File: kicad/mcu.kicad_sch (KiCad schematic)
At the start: 32 parts, among them J8 USB_C_Receptacle_USB2.0_14P, J9 Conn_01x03, SW1 SW_Push, SW2 SW_Push, U12 ESP32-S3-WROOM-1-N8R2

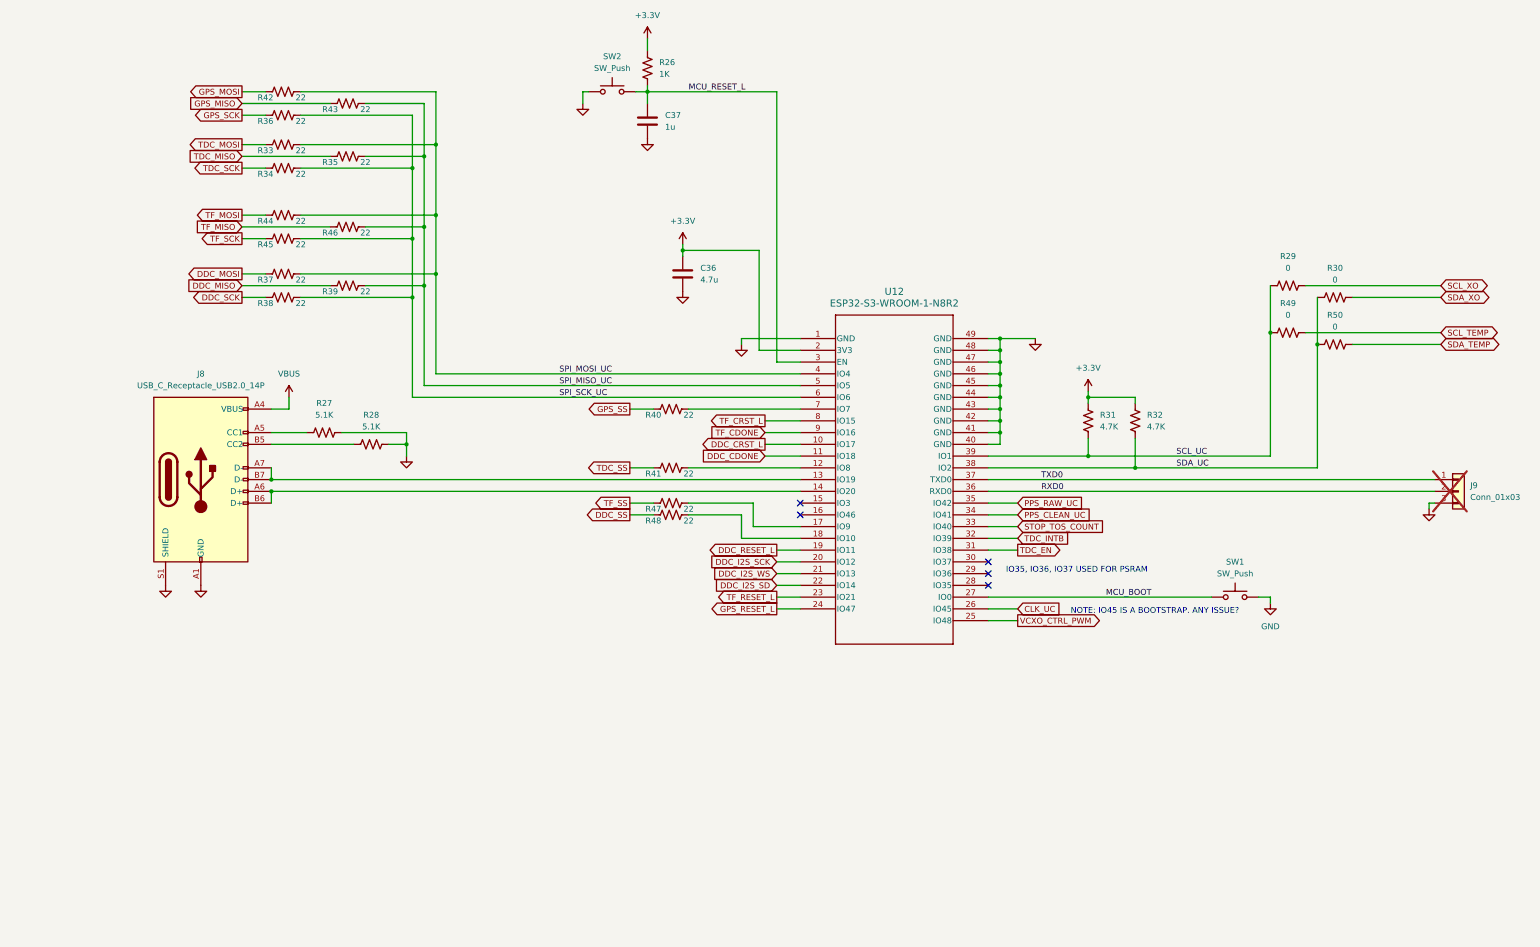
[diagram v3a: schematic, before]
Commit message: add tcxo
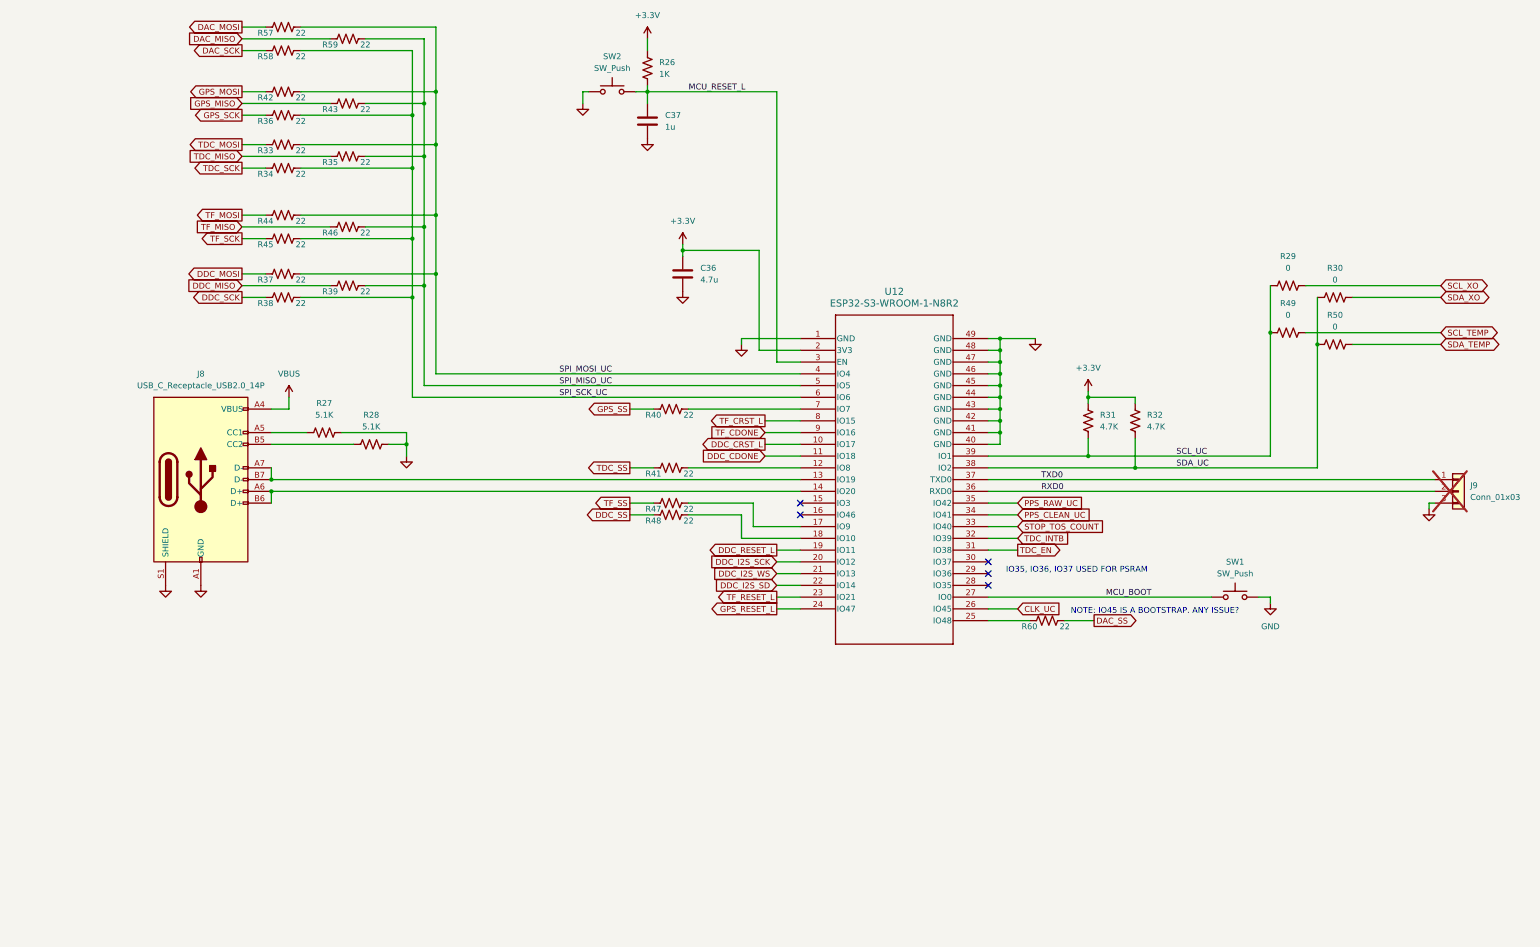
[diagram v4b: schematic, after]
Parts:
- added R57, R58, R59, R60: 22, symbol Device:R_US
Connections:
- net SPI_MISO_UC: now also R59.2
- net SPI_MOSI_UC: now also R57.2
- net SPI_SCK_UC: now also R58.2
- net VCXO_CTRL_PWM: no longer names the net of U12.25 (IO48)
- net VCXO_CTRL_PWM: now also R60.1
- new net DAC_MISO: R59.1
- new net DAC_MOSI: R57.1
- new net DAC_SCK: R58.1
- new net DAC_SS: R60.2
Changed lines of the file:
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@@
   (junction (at 229.87 120.65) (diameter 0) (color 0 0 0 0)
   )
+  (junction (at 105.41 54.61) (diameter 0) (color 0 0 0 0)
+  )
+  (junction (at 102.87 57.15) (diameter 0) (color 0 0 0 0)
+  )
   (junction (at 229.87 110.49) (diameter 0) (color 0 0 0 0)
   )
@@
   )
   (junction (at 248.92 130.81) (diameter 0) (color 0 0 0 0)
+  )
+  (junction (at 107.95 52.07) (diameter 0) (color 0 0 0 0)
   )
   (junction (at 102.87 68.58) (diameter 0) (color 0 0 0 0)
@@
     (stroke (width 0) (type default))
   )
+  (wire (pts (xy 66.04 38.1) (xy 71.12 38.1))
+    (stroke (width 0) (type default))
+  )
   (wire (pts (xy 227.33 125.73) (xy 229.87 125.73))
     (stroke (width 0) (type default))
@@
     (stroke (width 0) (type default))
   )
+  (wire (pts (xy 66.04 43.18) (xy 71.12 43.18))
+    (stroke (width 0) (type default))
+  )
   (wire (pts (xy 181.61 52.07) (xy 181.61 110.49))
     (stroke (width 0) (type default))
@@
     (stroke (width 0) (type default))
   )
+  (wire (pts (xy 227.33 166.37) (xy 236.22 166.37))
+    (stroke (width 0) (type default))
+  )
   (wire (pts (xy 151.13 52.07) (xy 153.67 52.07))
     (stroke (width 0) (type default))
@@
     (stroke (width 0) (type default))
   )
+  (wire (pts (xy 92.71 40.64) (xy 105.41 40.64))
+    (stroke (width 0) (type default))
+  )
   (wire (pts (xy 177.8 107.95) (xy 177.8 86.36))
     (stroke (width 0) (type default))
@@
     (stroke (width 0) (type default))
   )
-  (wire (pts (xy 227.33 166.37) (xy 233.68 166.37))
-    (stroke (width 0) (type default))
-  )
   (wire (pts (xy 298.45 133.35) (xy 259.08 133.35))
     (stroke (width 0) (type default))
@@
     (stroke (width 0) (type default))
   )
+  (wire (pts (xy 107.95 38.1) (xy 107.95 52.07))
+    (stroke (width 0) (type default))
+  )
   (wire (pts (xy 72.39 138.43) (xy 186.69 138.43))
     (stroke (width 0) (type default))
   )
+  (wire (pts (xy 105.41 40.64) (xy 105.41 54.61))
+    (stroke (width 0) (type default))
+  )
   (wire (pts (xy 227.33 148.59) (xy 233.68 148.59))
     (stroke (width 0) (type default))
@@
     (stroke (width 0) (type default))
   )
+  (wire (pts (xy 66.04 40.64) (xy 85.09 40.64))
+    (stroke (width 0) (type default))
+  )
   (wire (pts (xy 78.74 91.44) (xy 107.95 91.44))
     (stroke (width 0) (type default))
@@
     (stroke (width 0) (type default))
   )
+  (wire (pts (xy 78.74 43.18) (xy 102.87 43.18))
+    (stroke (width 0) (type default))
+  )
+  (wire (pts (xy 102.87 43.18) (xy 102.87 57.15))
+    (stroke (width 0) (type default))
+  )
   (wire (pts (xy 78.74 78.74) (xy 107.95 78.74))
     (stroke (width 0) (type default))
@@
     (stroke (width 0) (type default))
   )
+  (wire (pts (xy 243.84 166.37) (xy 250.19 166.37))
+    (stroke (width 0) (type default))
+  )
   (wire (pts (xy 78.74 63.5) (xy 107.95 63.5))
     (stroke (width 0) (type default))
@@
   )
   (wire (pts (xy 229.87 110.49) (xy 229.87 107.95))
+    (stroke (width 0) (type default))
+  )
+  (wire (pts (xy 78.74 38.1) (xy 107.95 38.1))
     (stroke (width 0) (type default))
   )
@@
     )
   )
+  (global_label "DAC_SCK" (shape output) (at 66.04 43.18 180) (fields_autoplaced)
+    (effects (font (size 1.27 1.27)) (justify right))
+    (property "Intersheetrefs" "${INTERSHEET_REFS}" (at 54.7091 43.18 0)
+      (effects (font (size 1.27 1.27)) (justify right) hide)
+    )
+  )
   (global_label "TDC_SCK" (shape output) (at 66.04 68.58 180) (fields_autoplaced)
     (effects (font (size 1.27 1.27)) (justify right))
@@
     )
   )
-  (global_label "VCXO_CTRL_PWM" (shape output) (at 233.68 166.37 0) (fields_autoplaced)
+  (global_label "DAC_SS" (shape output) (at 250.19 166.37 0) (fields_autoplaced)
     (effects (font (size 1.27 1.27)) (justify left))
-    (property "Intersheetrefs" "${INTERSHEET_REFS}" (at 252.2075 166.37 0)
+    (property "Intersheetrefs" "${INTERSHEET_REFS}" (at 260.1904 166.37 0)
       (effects (font (size 1.27 1.27)) (justify left) hide)
     )
@@
     (effects (font (size 1.27 1.27)) (justify right))
     (property "Intersheetrefs" "${INTERSHEET_REFS}" (at 53.7415 54.61 0)
+      (effects (font (size 1.27 1.27)) (justify right) hide)
+    )
+  )
+  (global_label "DAC_MISO" (shape input) (at 66.04 40.64 180) (fields_autoplaced)
+    (effects (font (size 1.27 1.27)) (justify right))
+    (property "Intersheetrefs" "${INTERSHEET_REFS}" (at 53.8624 40.64 0)
       (effects (font (size 1.27 1.27)) (justify right) hide)
     )
@@
     (effects (font (size 1.27 1.27)) (justify right))
     (property "Intersheetrefs" "${INTERSHEET_REFS}" (at 54.5277 96.52 0)
+      (effects (font (size 1.27 1.27)) (justify right) hide)
+    )
+  )
+  (global_label "DAC_MOSI" (shape output) (at 66.04 38.1 180) (fields_autoplaced)
+    (effects (font (size 1.27 1.27)) (justify right))
+    (property "Intersheetrefs" "${INTERSHEET_REFS}" (at 53.8624 38.1 0)
       (effects (font (size 1.27 1.27)) (justify right) hide)
     )
@@
     )
   )
+  (symbol (lib_id "Device:R_US") (at 240.03 166.37 90) (unit 1)
+    (in_bom yes) (on_board yes) (dnp no)
+    (property "Reference" "R60" (at 236.22 167.64 90)
+      (effects (font (size 1.27 1.27)))
+    )
+    (property "Value" "22" (at 243.84 167.64 90)
+      (effects (font (size 1.27 1.27)))
+    )
+    (property "Footprint" "" (at 240.284 165.354 90)
+      (effects (font (size 1.27 1.27)) hide)
+    )
+    (property "Datasheet" "~" (at 240.03 166.37 0)
+      (effects (font (size 1.27 1.27)) hide)
+    )
+    (pin "1")
+    (pin "2")
+    (instances
+      (project "gpsrx"
+        (path "/c3c549bc-9d82-4b6a-bdb9-a3870905229d/cfc19a79-2a34-431b-9452-a8a8f8302b67"
+          (reference "R60") (unit 1)
+        )
+      )
+    )
+  )
   (symbol (lib_id "power:GND") (at 57.15 158.75 0) (unit 1)
     (in_bom yes) (on_board yes) (dnp no) (fields_autoplaced)
@@
         (path "/c3c549bc-9d82-4b6a-bdb9-a3870905229d/cfc19a79-2a34-431b-9452-a8a8f8302b67"
           (reference "SW1") (unit 1)
+        )
+      )
+    )
+  )
+  (symbol (lib_id "Device:R_US") (at 88.9 40.64 90) (unit 1)
+    (in_bom yes) (on_board yes) (dnp no)
+    (property "Reference" "R59" (at 85.09 41.91 90)
+      (effects (font (size 1.27 1.27)))
+    )
+    (property "Value" "22" (at 92.71 41.91 90)
+      (effects (font (size 1.27 1.27)))
+    )
+    (property "Footprint" "" (at 89.154 39.624 90)
+      (effects (font (size 1.27 1.27)) hide)
+    )
+    (property "Datasheet" "~" (at 88.9 40.64 0)
+      (effects (font (size 1.27 1.27)) hide)
+    )
+    (pin "1")
+    (pin "2")
+    (instances
+      (project "gpsrx"
+        (path "/c3c549bc-9d82-4b6a-bdb9-a3870905229d/cfc19a79-2a34-431b-9452-a8a8f8302b67"
+          (reference "R59") (unit 1)
         )
       )
@@
     )
   )
+  (symbol (lib_id "Device:R_US") (at 74.93 38.1 90) (unit 1)
+    (in_bom yes) (on_board yes) (dnp no)
+    (property "Reference" "R57" (at 71.12 39.37 90)
+      (effects (font (size 1.27 1.27)))
+    )
+    (property "Value" "22" (at 78.74 39.37 90)
+      (effects (font (size 1.27 1.27)))
+    )
+    (property "Footprint" "" (at 75.184 37.084 90)
+      (effects (font (size 1.27 1.27)) hide)
+    )
+    (property "Datasheet" "~" (at 74.93 38.1 0)
+      (effects (font (size 1.27 1.27)) hide)
+    )
+    (pin "1")
+    (pin "2")
+    (instances
+      (project "gpsrx"
+        (path "/c3c549bc-9d82-4b6a-bdb9-a3870905229d/cfc19a79-2a34-431b-9452-a8a8f8302b67"
+          (reference "R57") (unit 1)
+        )
+      )
+    )
+  )
   (symbol (lib_id "Device:R_US") (at 292.1 104.14 90) (unit 1)
     (in_bom yes) (on_board yes) (dnp no) (fields_autoplaced)
@@
         )
       )
+    )
+  )
+  (symbol (lib_id "Device:R_US") (at 74.93 43.18 90) (unit 1)
+    (in_bom yes) (on_board yes) (dnp no)
+    (property "Reference" "R58" (at 71.12 44.45 90)
+      (effects (font (size 1.27 1.27)))
+    )
+    (property "Value" "22" (at 78.74 44.45 90)
+      (effects (font (size 1.27 1.27)))
+    )
+    (property "Footprint" "" (at 75.184 42.164 90)
+      (effects (font (size 1.27 1.27)) hide)
+    )
+    (property "Datasheet" "~" (at 74.93 43.18 0)
+      (effects (font (size 1.27 1.27)) hide)
+    )
+    (pin "1")
+    (pin "2")
+    (instances
+      (project "gpsrx"
+        (path "/c3c549bc-9d82-4b6a-bdb9-a3870905229d/cfc19a79-2a34-431b-9452-a8a8f8302b67"
+          (reference "R58") (unit 1)
+        )
+      )

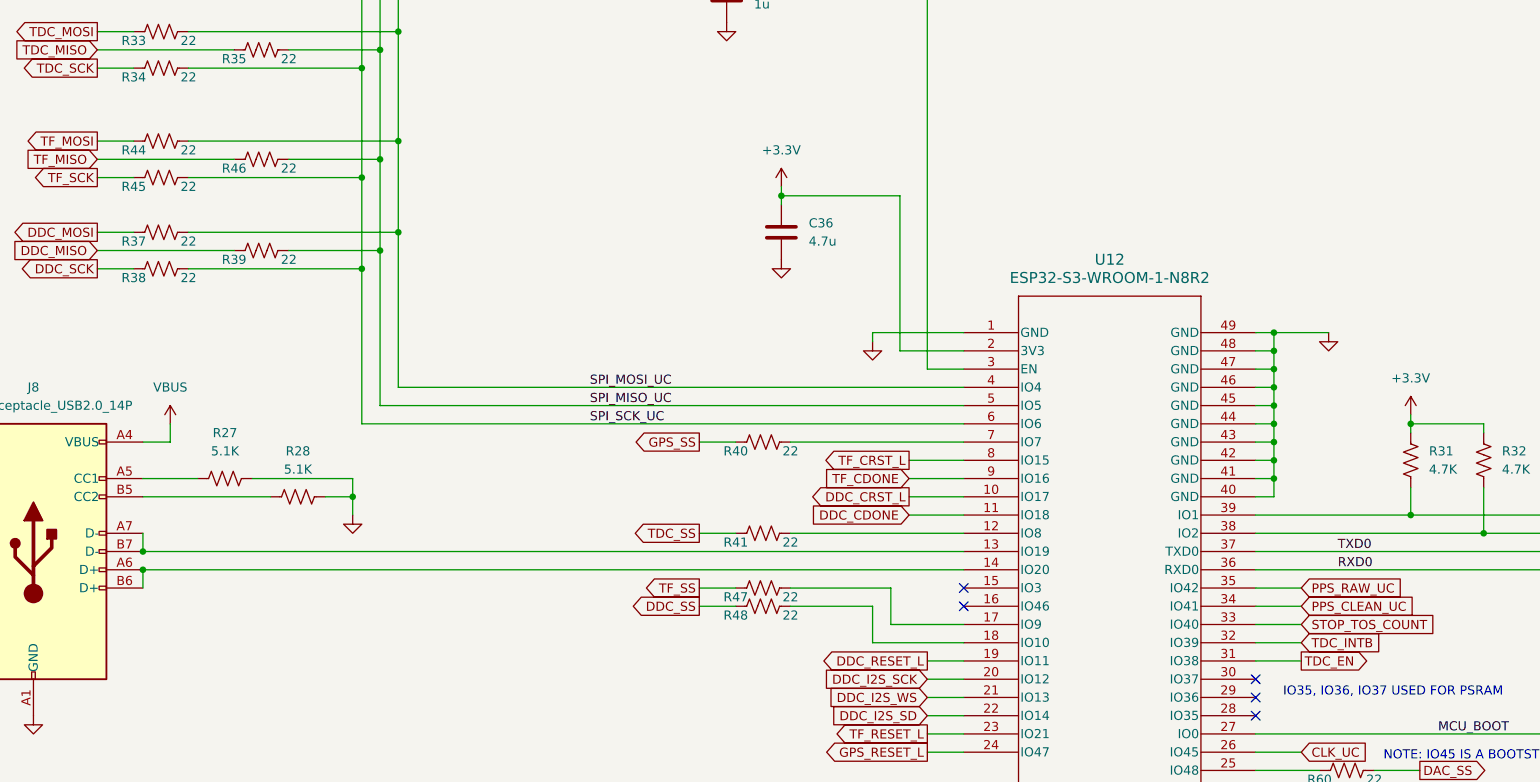
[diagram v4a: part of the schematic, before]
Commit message: swap ice40 for max v, add 1.2v switcher
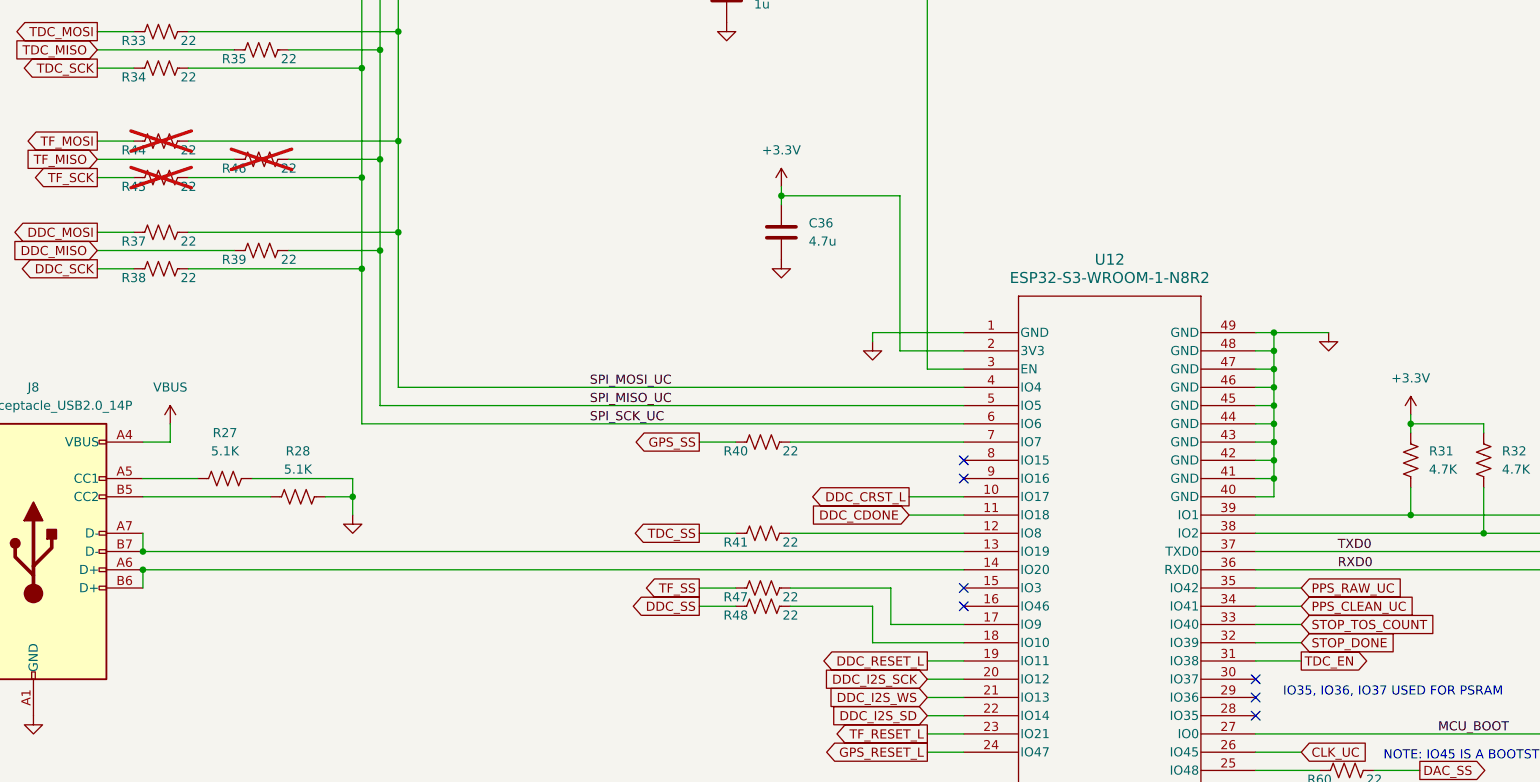
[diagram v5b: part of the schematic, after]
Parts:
- R44, R45, R46: now not fitted
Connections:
- net TDC_INTB renamed STOP_DONE
- net TF_CDONE: no longer names the net of U12.9 (IO16)
- net TF_CRST_L: no longer names the net of U12.8 (IO15)
- no-connect marks 5 -> 7
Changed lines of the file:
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@@
   (no_connect (at 227.33 158.75))
   (no_connect (at 227.33 156.21))
+  (no_connect (at 186.69 123.19))
   (no_connect (at 186.69 140.97))
   (no_connect (at 227.33 153.67))
+  (no_connect (at 186.69 125.73))
   (no_connect (at 186.69 143.51))
   (wire (pts (xy 248.92 118.11) (xy 248.92 119.38))
@@
     (stroke (width 0) (type default))
   )
-  (wire (pts (xy 179.07 123.19) (xy 186.69 123.19))
-    (stroke (width 0) (type default))
-  )
   (wire (pts (xy 66.04 63.5) (xy 71.12 63.5))
     (stroke (width 0) (type default))
@@
   )
   (wire (pts (xy 229.87 113.03) (xy 229.87 110.49))
-    (stroke (width 0) (type default))
-  )
-  (wire (pts (xy 179.07 125.73) (xy 186.69 125.73))
     (stroke (width 0) (type default))
   )
@@
     )
   )
-  (global_label "TF_CDONE" (shape input) (at 179.07 125.73 180) (fields_autoplaced)
-    (effects (font (size 1.27 1.27)) (justify right))
-    (property "Intersheetrefs" "${INTERSHEET_REFS}" (at 166.711 125.73 0)
-      (effects (font (size 1.27 1.27)) (justify right) hide)
-    )
-  )
   (global_label "TF_SCK" (shape output) (at 66.04 83.82 180) (fields_autoplaced)
     (effects (font (size 1.27 1.27)) (justify right))
@@
     )
   )
-  (global_label "TF_CRST_L" (shape output) (at 179.07 123.19 180) (fields_autoplaced)
-    (effects (font (size 1.27 1.27)) (justify right))
-    (property "Intersheetrefs" "${INTERSHEET_REFS}" (at 166.3482 123.19 0)
-      (effects (font (size 1.27 1.27)) (justify right) hide)
-    )
-  )
   (global_label "DDC_I2S_SCK" (shape input) (at 181.61 153.67 180) (fields_autoplaced)
     (effects (font (size 1.27 1.27)) (justify right))
@@
     )
   )
-  (global_label "TDC_INTB" (shape input) (at 233.68 148.59 0) (fields_autoplaced)
+  (global_label "STOP_DONE" (shape input) (at 233.68 148.59 0) (fields_autoplaced)
     (effects (font (size 1.27 1.27)) (justify left))
-    (property "Intersheetrefs" "${INTERSHEET_REFS}" (at 245.3133 148.59 0)
+    (property "Intersheetrefs" "${INTERSHEET_REFS}" (at 247.4904 148.59 0)
       (effects (font (size 1.27 1.27)) (justify left) hide)
     )
@@
   )
   (symbol (lib_id "Device:R_US") (at 74.93 83.82 90) (unit 1)
-    (in_bom yes) (on_board yes) (dnp no)
+    (in_bom yes) (on_board yes) (dnp yes)
     (property "Reference" "R45" (at 71.12 85.09 90)
       (effects (font (size 1.27 1.27)))
@@
   )
   (symbol (lib_id "Device:R_US") (at 74.93 78.74 90) (unit 1)
-    (in_bom yes) (on_board yes) (dnp no)
+    (in_bom yes) (on_board yes) (dnp yes)
     (property "Reference" "R44" (at 71.12 80.01 90)
       (effects (font (size 1.27 1.27)))
@@
   )
   (symbol (lib_id "Device:R_US") (at 88.9 81.28 90) (unit 1)
-    (in_bom yes) (on_board yes) (dnp no)
+    (in_bom yes) (on_board yes) (dnp yes)
     (property "Reference" "R46" (at 85.09 82.55 90)
       (effects (font (size 1.27 1.27)))
